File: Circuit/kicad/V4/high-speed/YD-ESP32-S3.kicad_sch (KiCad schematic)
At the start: 21 parts, among them Q2 bc akármi, Q3 bc akármi, U37 CH343P

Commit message: V4.1.7 PSU  V1.0 debug Card
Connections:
- net BMO_INT: no longer ESP1.17 (IO9)
- net I2C_CH: no longer ESP1.31 (IO38)
- net I2C_MUX/ESP_I2C_SCL_sensors: no longer ESP1.35 (MTMS/IO42)
- net I2C_MUX/ESP_I2C_SDA_sensors: no longer ESP1.34 (MTDI/IO41)
- net INA226_ALERT: no longer ESP1.18 (IO10)
- net M1_step: no longer ESP1.39 (IO1)
- net M2_step: no longer ESP1.38 (IO2)
- net M3_step: no longer ESP1.15 (IO3)
- net M4_step: no longer ESP1.4 (IO4)
- net MCP_RST: no longer ESP1.6 (IO6)
- net PWMA: no longer ESP1.7 (IO7)
- net PWMB: no longer ESP1.12 (IO8)
- net RPI_UART_RX: no longer ESP1.11 (IO18)
- net RPI_UART_TX: no longer ESP1.10 (IO17)
- net SPI2_CH: no longer ESP1.33 (MTDO/IO40)
- net SPI_TMC_CH: no longer ESP1.32 (MTCK/IO39)
- net WS_2802B_DATA: no longer ESP1.23 (IO21)
- net ESP_GPIO45: no longer names the net of ESP1.26 (IO45)
- net ESP_GPIO46: no longer names the net of ESP1.16 (IO46)
- net ESP_GPIO47: no longer names the net of ESP1.24 (IO47)
- net ESP_GPIO48: no longer names the net of ESP1.25 (IO48)
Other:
- moved on the sheet: C81, C82, C83, CT3

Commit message: high speed first step
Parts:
- removed ESP1: ESP32-S3-WROOM-2, RF_Module:ESP32-S3-WROOM-2, symbol RF_Module:ESP32-S3-WROOM-2
- added SPI1, SPI2, SPI3, SPI4: Conn_01x06_Socket, Connector_JST:JST_PH_B6B-PH-K_1x06_P2.00mm_Vertical, symbol Connector:Conn_01x06_Socket
- added TP36, TP37, TP38: TestPoint_Small, symbol Connector:TestPoint_Small
- added U18: ESP32-S3-WROOM-1, RF_Module:ESP32-S3-WROOM-1, symbol RF_Module:ESP32-S3-WROOM-1
- added U19: MCP23S17_SO, Package_SO:SSOP-28_3.9x9.9mm_P0.635mm, symbol Interface_Expansion:MCP23S17_SO
- added U20: CD74HC154M, Package_SO:SOIC-24W_7.5x15.4mm_P1.27mm, symbol 74HC154:CD74HC154M
- renumbered C84 to C37, C78 to C38, C79 to C39, C80 to C40, C81 to C41, C82 to C42, C83 to C43, CT3 to CT5, D4 to D7, Q3 to Q1, R70 to R64, R71 to R65, R69 to R66, R72 to R67, R73 to R68, R74 to R69, U37 to U17
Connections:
- net 3v3-input: now also SPI1.1 (Pin_1), SPI2.1 (Pin_1), SPI3.1 (Pin_1), SPI4.1 (Pin_1), U18.2 (3V3)
- net ESP_usbD+: now also U18.14 (USB_D+)
- net ESP_usbD-: now also U18.13 (USB_D-)
- net GND: now also SPI1.6 (Pin_6), SPI2.6 (Pin_6), SPI3.6 (Pin_6), SPI4.6 (Pin_6), U18.1 (GND), U18.40 (GND), U18.41 (GND), U19.10 (VSS), U19.16 (A1), U19.17 (A2), U20.12 (GND)
- net I2C_CH: now also U18.18 (IO10), U19.7 (GPB6)
- net M1_step: now also U18.4 (IO4)
- net M2_step: now also U18.5 (IO5)
- net M3_step: now also U18.6 (IO6)
- net M4_step: now also U18.7 (IO7)
- net MCP_CS: now also U20.14 (~{Y12})
- net MCP_RST: now also U18.15 (IO3), U19.18 (~{RESET}), U19.6 (GPB5)
- net PWMA: now also U18.39 (IO1)
- net PWMB: now also U18.38 (IO2)
- net WS_2802B_DATA: now also U18.23 (IO21)
- net esp32_chip_pu: now also U18.3 (EN)
- net esp32_gpio0: now also U18.27 (IO0)
- net esp_rxd0: now also U18.36 (RXD0)
- net esp_txd0: now also U18.37 (TXD0)
- new net: TP37.1, U18.29 (IO36)
- new net: TP36.1, U18.28 (IO35)
- new net: TP38.1, U18.30 (IO37)
- new net 5V: U19.15 (A0)
- new net AIN1: U19.25 (GPA4)
- new net AIN2: U19.26 (GPA5)
- new net BIN1: U19.27 (GPA6)
- new net BIN2: U19.28 (GPA7)
- new net BNO_INT: U18.8 (IO15)
- new net CS: U19.11 (~{CS})
- new net CS_S_A0: U18.26 (IO45), U20.23 (A0)
- new net CS_S_A1: U18.16 (IO46), U20.22 (A1)
- new net CS_S_A2: U18.24 (IO47), U20.21 (A2)
- new net CS_S_A3: U18.25 (IO48), U20.20 (A3)
- new net ESP_3v3: U19.9 (VDD), U20.18 (E1), U20.19 (E2), U20.24 (VCC)
- new net ESP_SEN_I2C_SCL: U18.17 (IO9)
- new net ESP_SEN_I2C_SDA: U18.12 (IO8)
- new net ESP_UART_RX: U18.10 (IO17)
- new net ESP_UART_TX: U18.11 (IO18)
- new net I2C_RST: U19.8 (GPB7)
- new net ICM_INT: U18.9 (IO16)
- new net M1_CS: U19.21 (GPA0), U20.9 (~{Y8})
- new net M2_CS: U19.22 (GPA1), U20.10 (~{Y9})
- new net M3_CS: U19.23 (GPA2), U20.11 (~{Y10})
- new net M4_CS: U19.24 (GPA3), U20.13 (~{Y11})
- new net MISO: U19.14 (SO)
- new net MOSI: U19.13 (SI)
- new net RPI-ESP_INT: U18.35 (IO42)
- new net RPI_CS: U18.22 (IO14)
- new net RPI_MISO: U18.20 (IO12)
- new net RPI_MOSI: U18.21 (IO13)
- new net RPI_SPI_CLK: U18.19 (IO11)
- new net SENSOR_CS: U18.33 (IO40)
- new net SENSOR_MISO: SPI1.3 (Pin_3), SPI2.3 (Pin_3), SPI3.3 (Pin_3), SPI4.3 (Pin_3), U18.32 (IO39)
- new net SENSOR_MOSI: SPI1.4 (Pin_4), SPI2.4 (Pin_4), SPI3.4 (Pin_4), SPI4.4 (Pin_4), U18.31 (IO38)
- new net SENSOR_SPI_CLK: SPI1.2 (Pin_2), SPI2.2 (Pin_2), SPI3.2 (Pin_2), SPI4.2 (Pin_2), U18.34 (IO41)
- new net SPI_CLK: U19.12 (SCK)
- new net SPI_CS_1: U20.1 (~{Y0})
- new net SPI_CS_2: U20.2 (~{Y1})
- new net SPI_CS_3: U20.3 (~{Y2})
- new net SPI_CS_4: U20.4 (~{Y3})
- new net SPI_CS_5: SPI4.5 (Pin_5), U20.5 (~{Y4})
- new net SPI_CS_6: SPI3.5 (Pin_5), U20.6 (~{Y5})
- new net SPI_CS_7: SPI2.5 (Pin_5), U20.7 (~{Y6})
- new net SPI_CS_8: SPI1.5 (Pin_5), U20.8 (~{Y7})
- no-connect marks 5 -> 7
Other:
- removed sheet I2C_MUX
- removed sheet I2C_devices
- removed sheet SPI_devices
- removed sheet Shift_registers
- added sheet BME280 (BME280.kicad_sch)
- added sheet BMO085 (BNO085.kicad_sch)
- added sheet ICM-45686 (ICM-45686.kicad_sch)
- added sheet MCP3208 (MCP3208.kicad_sch)
- moved on the sheet: C37, C41, C42, C43, CT5, Q1, Q2, R68, R69, U17

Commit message: kicad: high speed V2.2 Circuit finish psu bom update
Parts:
- removed C39: 100nf, Capacitor_SMD:C_0805_2012Metric, symbol Device:C
- removed C41, C42, C43: 1uf, Capacitor_SMD:C_0805_2012Metric, symbol Device:C
- removed Q1, Q2: bc akármi, Package_TO_SOT_SMD:SOT-23, symbol Transistor_BJT:BC817
- removed R66: 1k, Resistor_SMD:R_0805_2012Metric, symbol Device:R
- removed R68, R69: 10k, Resistor_SMD:R_0805_2012Metric, symbol Device:R
- removed U17: CH343P, Package_DFN_QFN:QFN-16-1EP_3x3mm_P0.5mm_EP1.7x1.7mm_ThermalVias, symbol wch_mcu_peripheral:CH343P
- added C36: 1uf, Capacitor_SMD:C_0805_2012Metric, symbol Device:C
- added CT7: 100uF, Capacitor_Tantalum_SMD:CP_EIA-7343-31_Kemet-D, symbol Device:C_Polarized_Small
- added D10, D8, D9: LED, Diode_SMD:D_1206_3216Metric, symbol Device:LED
- added J14: RGB-BTN, symbol Connector:Conn_01x06_Socket
- added R133, R134, R135, R96: 1K, Resistor_SMD:R_0805_2012Metric, symbol Device:R
- added TP15: MCP_GPB_4, TestPoint:TestPoint_Pad_D2mm, symbol Connector:TestPoint_Small
- added TP16: MCP_GPB_5, TestPoint:TestPoint_Pad_D2mm, symbol Connector:TestPoint_Small
- added TP17: MCP_GPB_6, TestPoint:TestPoint_Pad_D2mm, symbol Connector:TestPoint_Small
- added TP18: MCP_GPB_7, TestPoint:TestPoint_Pad_D2mm, symbol Connector:TestPoint_Small
- C35: renamed from C40; Cikkszám (none) -> 100.277.53; Link (none) -> https://www.hestore.hu/prod_10027753.html
- C37: Cikkszám (none) -> 100.011.22; Link (none) -> https://www.hestore.hu/prod_10001122.html
- C38: value 100uf -> 22nf c0g; footprint Capacitor_Tantalum_SMD:CP_EIA-7343-31_Kemet-D -> Capacitor_SMD:C_0805_2012Metric; Cikkszám (none) -> 100.011.30; Link (none) -> https://www.hestore.hu/prod_10001130.html
- CT8: renamed from CT5; value 100uf -> 100uF; Cikkszám (none) -> 100.286.19; Link (none) -> https://www.hestore.hu/prod_10028619.html
- D5, D6, D7: Cikkszám (none) -> 100.365.89; Link (none) -> https://www.hestore.hu/prod_10048914.html
- R93: renamed from R64; value 1k -> 1K; Cikkszám (none) -> 100.011.57; Link (none) -> https://www.hestore.hu/prod_10001157.html
- R94: renamed from R65; value 1k -> 1K; Cikkszám (none) -> 100.011.57; Link (none) -> https://www.hestore.hu/prod_10001157.html
- R95: renamed from R67; value 10k -> 10K; Cikkszám (none) -> 100.011.45; Link (none) -> https://www.hestore.hu/prod_10001145.html
- SPI1, SPI2, SPI3, SPI4: Cikkszám (none) -> 100.491.16; Link (none) -> https://www.hestore.hu/prod_10049116.html
- TP10: renamed from TP37; footprint (none) -> TestPoint:TestPoint_Pad_D1.5mm; Cikkszám (none) -> -; Link (none) -> -; now left out of the parts list
- TP11: renamed from TP38; footprint (none) -> TestPoint:TestPoint_Pad_D1.5mm; Cikkszám (none) -> -; Link (none) -> -; now left out of the parts list
- TP9: renamed from TP36; footprint (none) -> TestPoint:TestPoint_Pad_D1.5mm; Cikkszám (none) -> -; Link (none) -> -; now left out of the parts list
- U19: renamed from U18; Cikkszám (none) -> 100.493.92; Link (none) -> https://www.hestore.hu/prod_10049392.html
- U20: renamed from U19; value MCP23S17_SO -> MCP23S17_SS; Cikkszám (none) -> 579-MCP23S17-E/SS; Link (none) -> https://hu.mouser.com/ProductDetail/Microchip-Technology/MC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
- U21: renamed from U20; Availability In Stock -> (none); Check_prices https://www.snapeda.com/parts/CD74HC154M/Texas+Instruments/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 -> (none); Cikkszám (none) -> 100.493.55; Description_1 High Speed CMOS Logic 4-to-16 Line Decoder/Demultiplexer -> (none); Link (none) -> https://www.hestore.hu/prod_10049355.html; MF Texas Instruments -> (none); MP CD74HC154M -> (none); Package SOIC-24 Texas Instruments -> (none); Price None -> (none); SnapEDA_Link https://www.snapeda.com/parts/CD74HC154M/Texas+Instruments/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 -> (none)
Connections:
- net 5V is gone; now on net 3v3-input: U20.15 (A0)
- net CS is gone; now on net MCP_CS: U20.11 (~{CS})
- net MISO is gone; now on net SENSOR_MOSI: U20.14 (SO)
- net MOSI is gone; now on net SENSOR_MISO: U20.13 (SI)
- net SPI_CLK is gone; now on net SENSOR_SPI_CLK: U20.12 (SCK)
- net esp32_gpio0 is gone; now on net RPI-ESP_INT: U19.27 (IO0)
- net 3v3-input: now also C37.2, C38.2, U20.9 (VDD), U21.24 (VCC), C36.2, CT7.1, J14.5 (Pin_5), R133.2, R134.2, R135.2; no longer C38.1
- net GND: now also C37.1, C38.1, U21.18 (E1), U21.19 (E2), C36.1, CT7.2, J14.1 (Pin_1); no longer C37.2, C38.2
- net I2C_CH: now also U20.23 (GPA2); no longer U20.7 (GPB6)
- net I2C_RST: now also U20.24 (GPA3); no longer U20.8 (GPB7)
- net M1_CS: no longer U20.21 (GPA0)
- net M2_CS: no longer U20.22 (GPA1)
- net M3_CS: no longer U20.23 (GPA2)
- net M4_CS: no longer U20.24 (GPA3)
- net MCP_RST: no longer U20.6 (GPB5)
- net RPI-ESP_INT: no longer U19.35 (IO42)
- net BTN_R: now reaches U20.1 (GPB0)
- net BTN_R: now also J14.2 (Pin_2)
- net MCP_IntB: now reaches U20.19 (INTB)
- net MCP_IntB: now also U19.35 (IO42)
- net BTN_G: now reaches U20.2 (GPB1)
- net BTN_G: now also J14.3 (Pin_3)
- net BTN_B: now reaches U20.3 (GPB2)
- net BTN_B: now also J14.4 (Pin_4)
- net BTN_ACT: now reaches U20.4 (GPB3)
- net BTN_ACT: now also J14.6 (Pin_6)
- net at U20.5 (GPB4): now also TP15.1
- net at D7.2 (A): now also R96.1
- net SPI_DIAG0: now reaches U21.15 (~{Y13})
- net SPI_DIAG0: now also D8.1 (K)
- net SPI_DIAG1: now reaches U21.16 (~{Y14})
- net SPI_DIAG1: now also D9.1 (K)
- net SPI_DIAG2: now reaches U21.17 (~{Y15})
- net SPI_DIAG2: now also D10.1 (K)
- removed net ESP_3v3: U20.9 (VDD), U21.18 (E1), U21.19 (E2), U21.24 (VCC)
- net esp32_chip_pu renamed ESP_RST
- net ESP_RST: now also R96.2
- new net: D8.2 (A), R133.1
- new net: TP17.1, U20.7 (GPB6)
- new net: TP16.1, U20.6 (GPB5)
- new net: TP18.1, U20.8 (GPB7)
- new net: D10.2 (A), R135.1
- new net: D9.2 (A), R134.1
- new net BNO_BOOT: U20.22 (GPA1)
- new net BNO_RST: U20.21 (GPA0)
- no-connect marks 7 -> 1
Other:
- sheet BMO085 ports: added 3V3; removed 3v3-input
- sheet MCP3208 ports: added 5v_to_ref; removed none
- moved on the sheet: C35, CT8, D5, D6, R93, R94, R95, TP10, TP11, TP9, U19

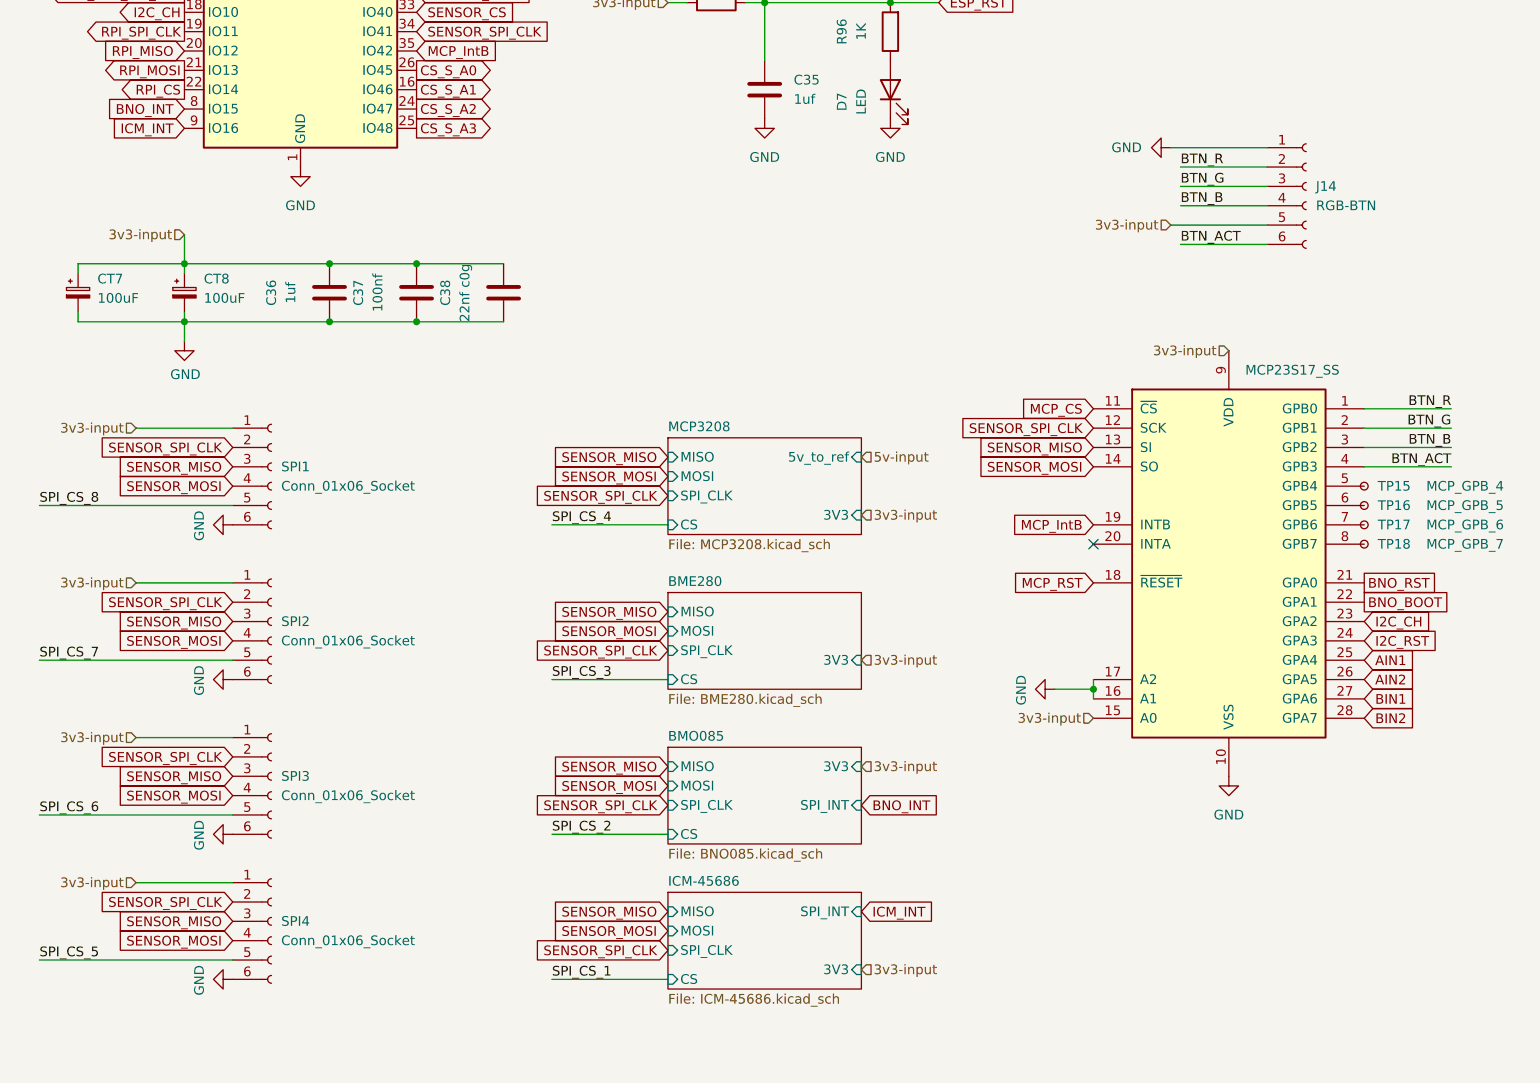
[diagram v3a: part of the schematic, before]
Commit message: finished high-speed panel schematic and first try to doute gpios
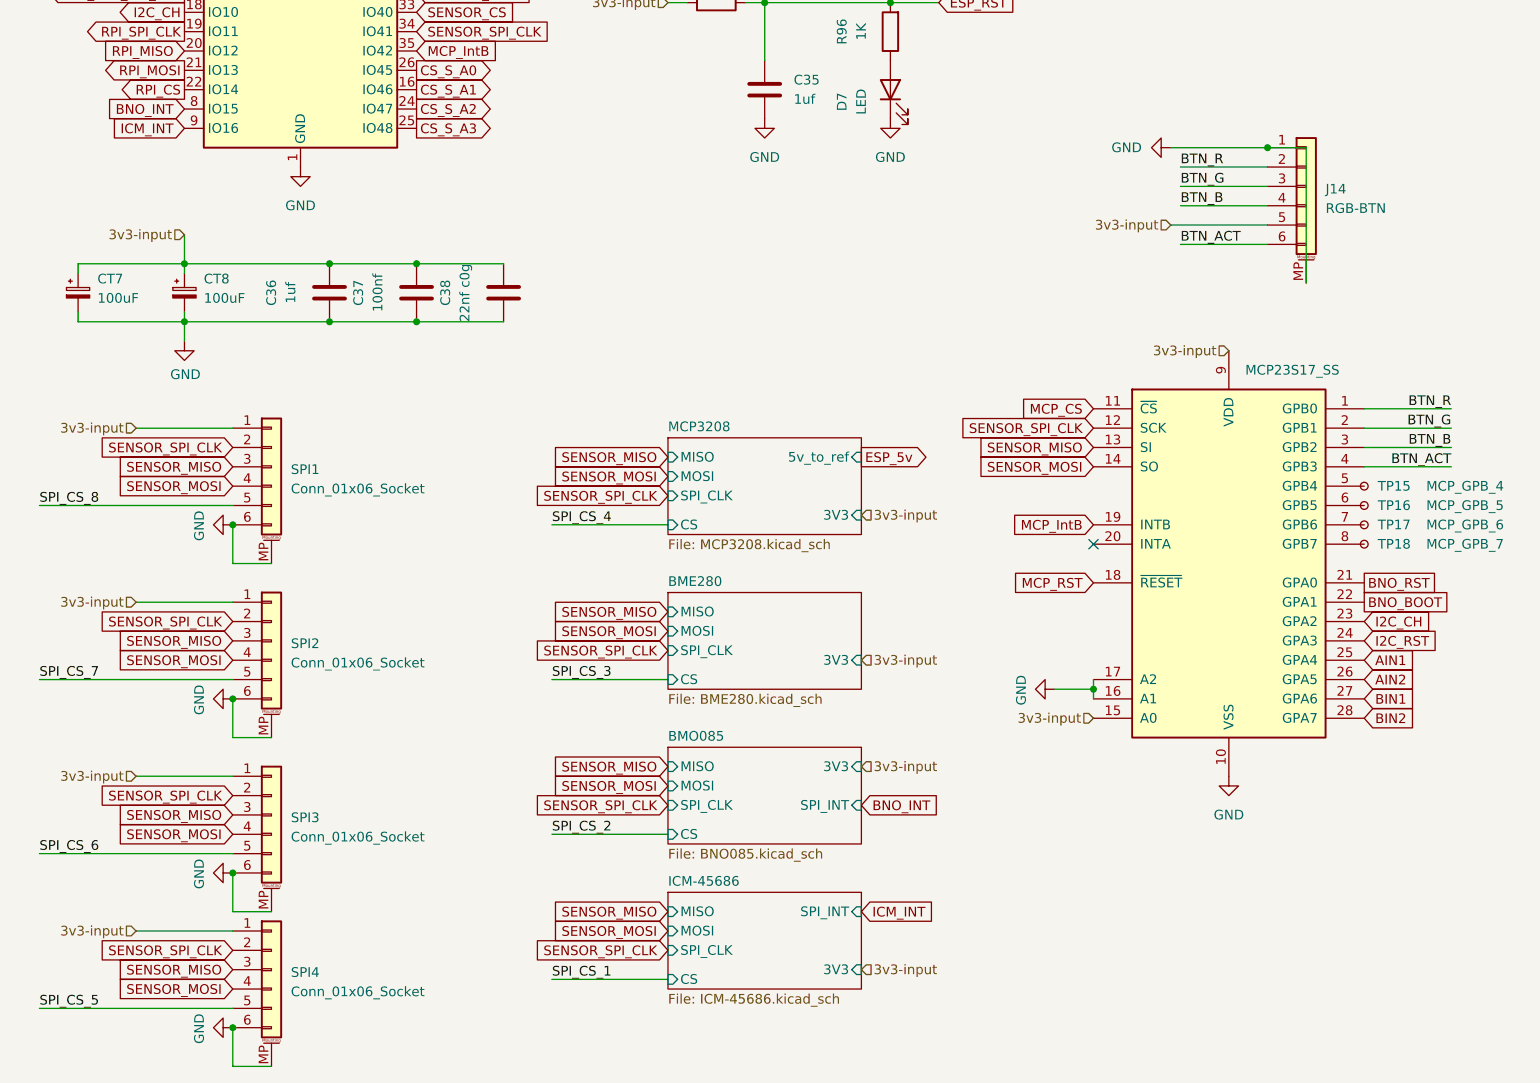
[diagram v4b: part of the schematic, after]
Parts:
- CT7, CT8: footprint Capacitor_Tantalum_SMD:CP_EIA-7343-31_Kemet-D -> Capacitor_Tantalum_SMD:CP_EIA-3528-21_Kemet-B
- J14: footprint (none) -> Connector_JST:JST_GH_BM06B-GHS-TBT_1x06-1MP_P1.25mm_Vertical; symbol Connector:Conn_01x06_Socket -> Connector_Generic_MountingPin:Conn_01x06_MountingPin
- SPI1, SPI2, SPI3, SPI4: footprint Connector_JST:JST_PH_B6B-PH-K_1x06_P2.00mm_Vertical -> Connector_JST:JST_GH_BM06B-GHS-TBT_1x06-1MP_P1.25mm_Vertical; symbol Connector:Conn_01x06_Socket -> Connector_Generic_MountingPin:Conn_01x06_MountingPin
- TP15, TP16, TP17, TP18: footprint TestPoint:TestPoint_Pad_D2mm -> TestPoint:TestPoint_Pad_D2.0mm
- U21: footprint Package_SO:SOIC-24W_7.5x15.4mm_P1.27mm -> Package_SO:TSSOP-24_4.4x7.8mm_P0.65mm
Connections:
- net GND: now also J14.MP (MountPin), SPI1.MP (MountPin), SPI2.MP (MountPin), SPI3.MP (MountPin), SPI4.MP (MountPin)
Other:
- moved on the sheet: J14, SPI1, SPI2, SPI3, SPI4
